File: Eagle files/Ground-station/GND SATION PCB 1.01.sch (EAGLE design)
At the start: 41 parts, among them IC1 BMP280, J6 503182-1852, U2 SOIC127P790X216-8NW25Q128JVJSQ

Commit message: Added USB-C and RESET button and corrections in Crystal Oscillator
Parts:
- added C17, C18, C19: 10uF, rcl:C-EUC0603
- added C20: 100nF, rcl:C-EUC0603
- added J1: USB4110GFA, USB4110GFA:USB4110GFA
- added R15, R16: 5.1k, rcl:R-EU_R0603
- added R17: 10k, rcl:R-EU_R0603
- added S2: DTS-3, DTS-3:DTS-3
- added U1: AMS1117-3.3, AMS1117-3.3:AMS1117-3.3
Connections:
- removed net N$10: C13.1
- removed net N$9: C14.1
- new net D_N: J1.DN1, J1.DN2, R10.2
- new net D_P: J1.DP1, J1.DP2, R9.2
- new net N$11: J1.CC1, R15.2
- new net N$13: C17.1, J1.VBUS, U1.VIN
- new net N$14: C20.1, R17.2, RP2040.RUN, S2.2
- new net N$15: J1.CC2, R16.2
- net +3V3: now also C18.1, C19.1, R17.1, U1.VOUT; no longer RP2040.RUN
- net 0: now also C13.1, C14.1, C17.2, C18.2, C19.2, C20.2, J1.GND, R15.1, R16.1, S2.1, U1.GND/ADJ
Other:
- moved on the sheet: C13, C14

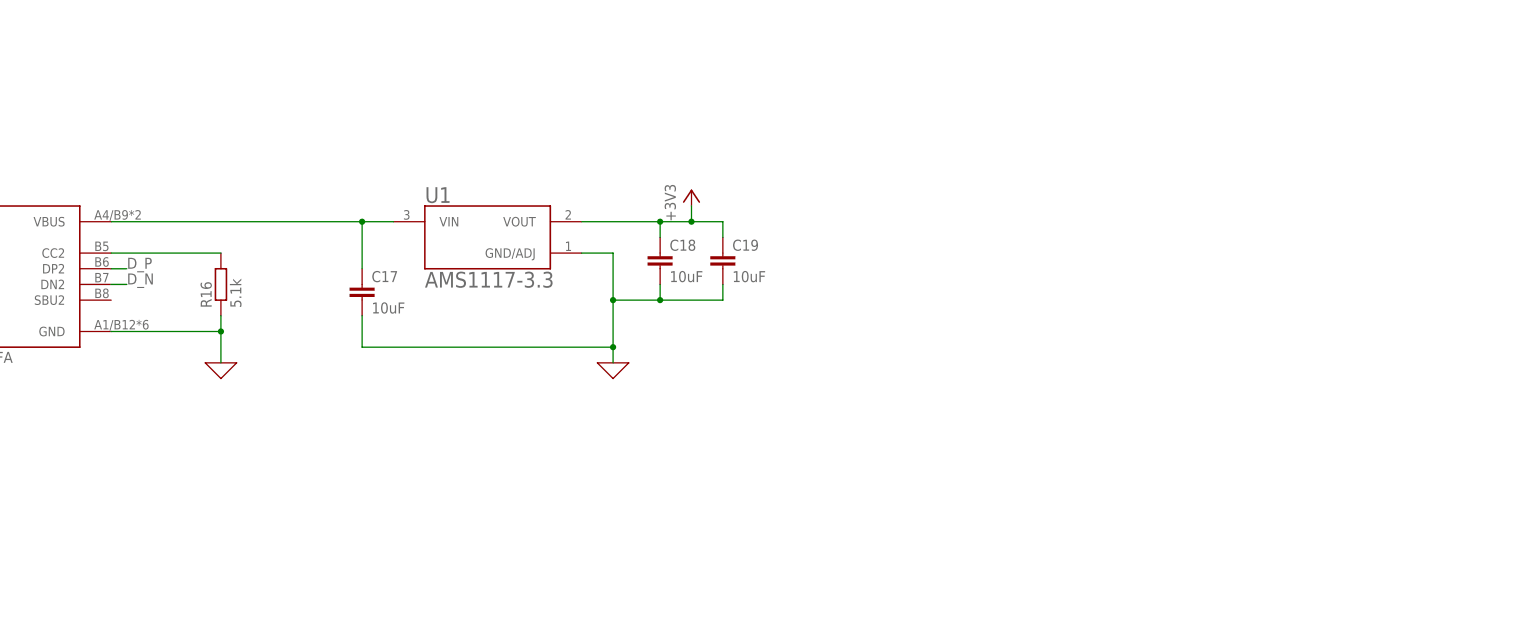
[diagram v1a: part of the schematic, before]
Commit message: Refined power design with Schottky diode multiplexer and Buck converter
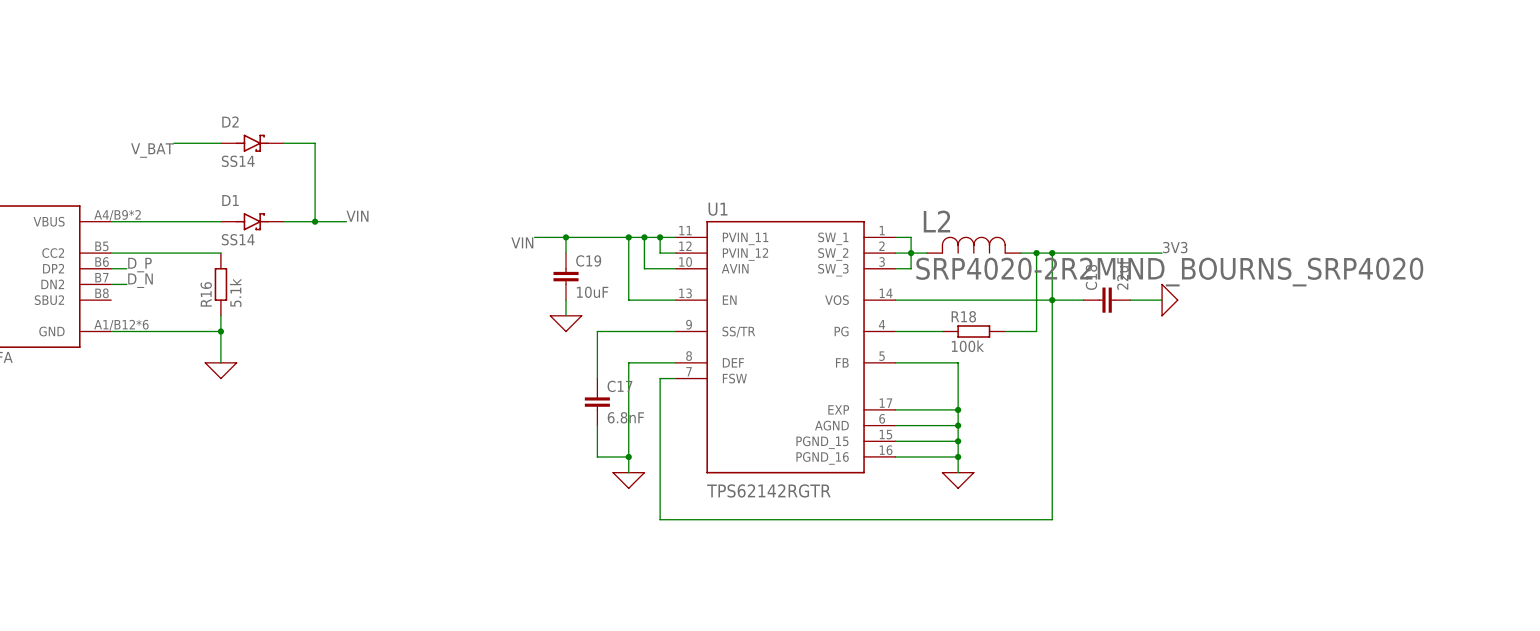
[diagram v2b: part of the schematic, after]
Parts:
- added D1, D2: SS14, SS14:SS14
- added L2: SRP4020-2R2MIND_BOURNS_SRP4020, SRP4020-2R2M:SRP4020-2R2MIND_BOURNS_SRP4020
- added R18: 100k, rcl:R-EU_R0603
- C17: value 10uF -> 6.8nF
- C18: value 10uF -> 22uF
- U1: value AMS1117-3.3 -> TPS62142RGTR; device AMS1117-3.3:AMS1117-3.3 -> TPS62142RGTR:TPS62142RGTR
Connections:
- removed net N$13: C17.1, J1.VBUS, U1.VIN
- new net 3V3: C18.1, L2.1, R18.2, U1.FSW, U1.VOS
- new net N$10: C17.1, U1.SS/TR
- new net N$17: L2.2, U1.SW_1, U1.SW_2, U1.SW_3
- new net N$20: R18.1, U1.PG
- new net N$9: D1.A, J1.VBUS
- new net VIN: C19.1, D1.K, D2.K, U1.AVIN, U1.EN, U1.PVIN_11, U1.PVIN_12
- new net V_BAT: D2.A
- net +3V3: no longer C18.1, C19.1, U1.VOUT
- net 0: now also U1.AGND, U1.DEF, U1.EXP, U1.FB, U1.PGND_15, U1.PGND_16; no longer U1.GND/ADJ
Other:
- moved on the sheet: C17, C18, C19
